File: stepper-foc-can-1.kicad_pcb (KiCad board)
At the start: 4 copper layers, 84 parts, among them J1 TC2030, J2 Conn_01x02, J3 Conn_01x04_Pin, J4 Conn_01x02, J5 Conn_01x02, M1 Stepper_Motor_bipolar, SW1 SW_Push, SW2 SW_Push, SW3 SW_Push, U1 STM32G474RBTx, U2 MX25947, U3 TPS62933, U4 TCAN3413, U5 AS5047P, U6 DRV8874, U7 INA241A3IDDF, U8 DRV8874, U9 INA241A3IDDF, Y1 Crystal_GND24

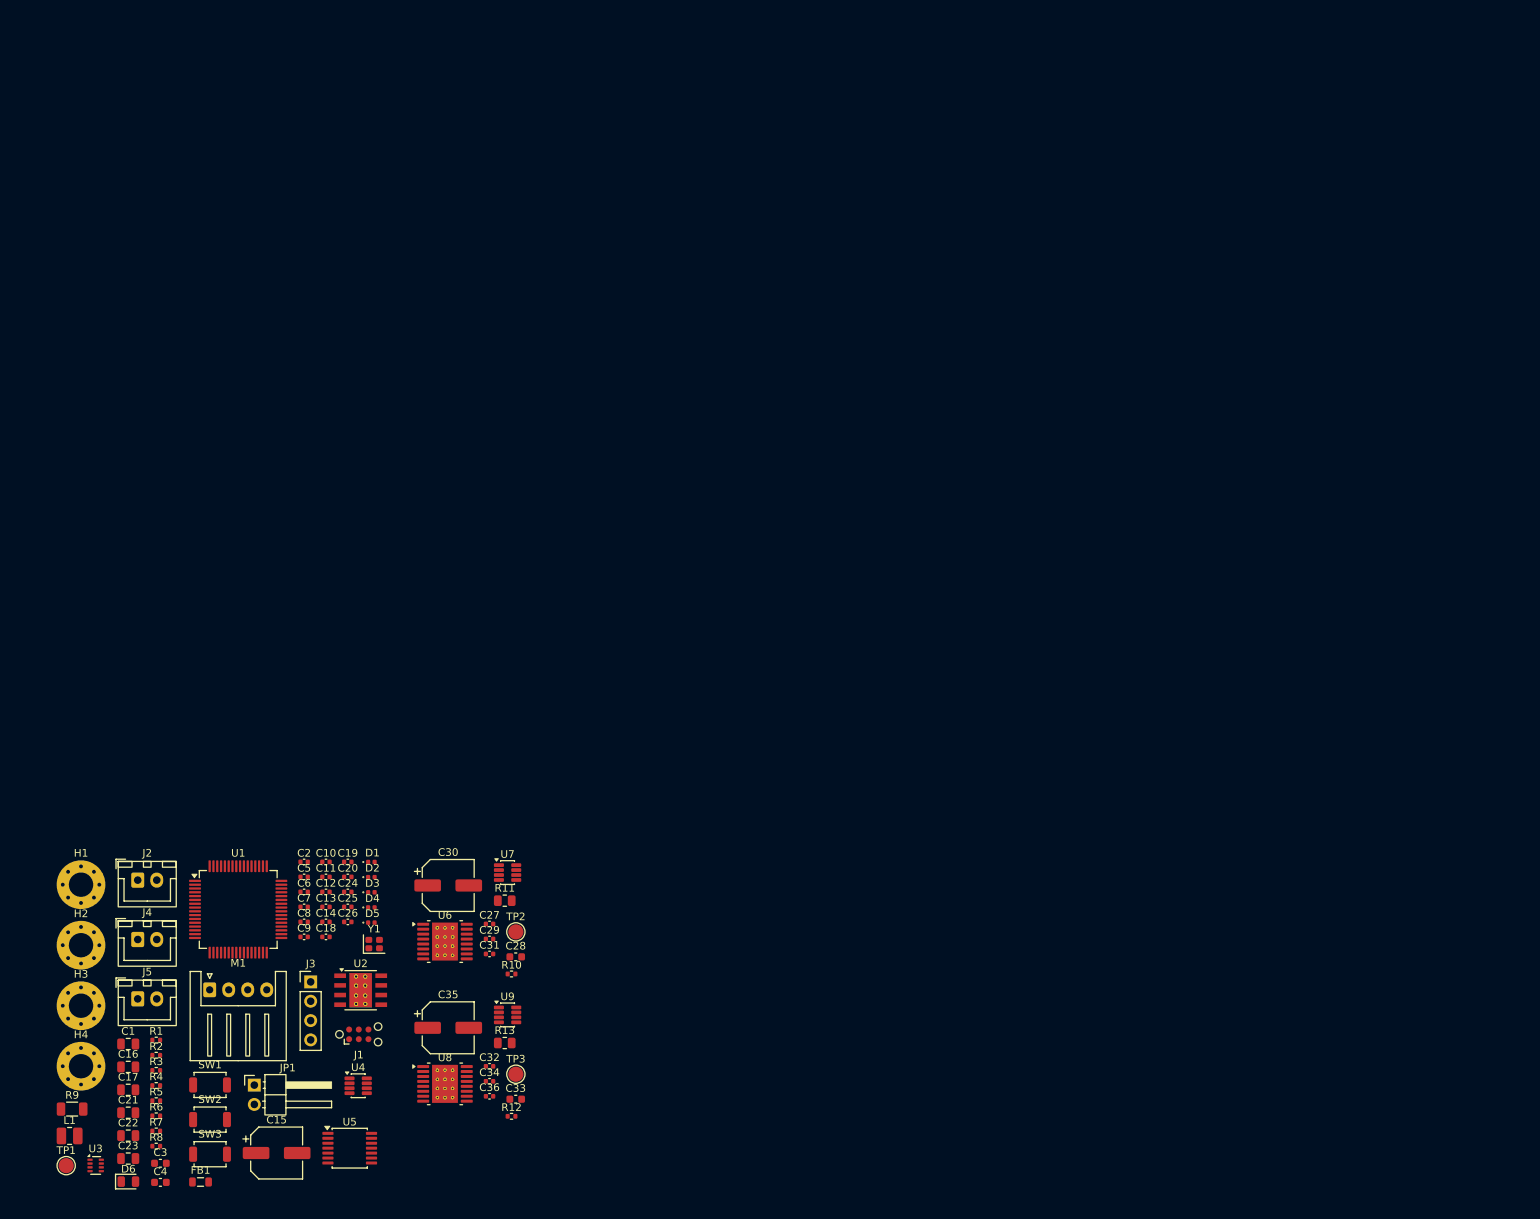
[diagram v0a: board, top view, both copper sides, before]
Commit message: pcb: add board outline
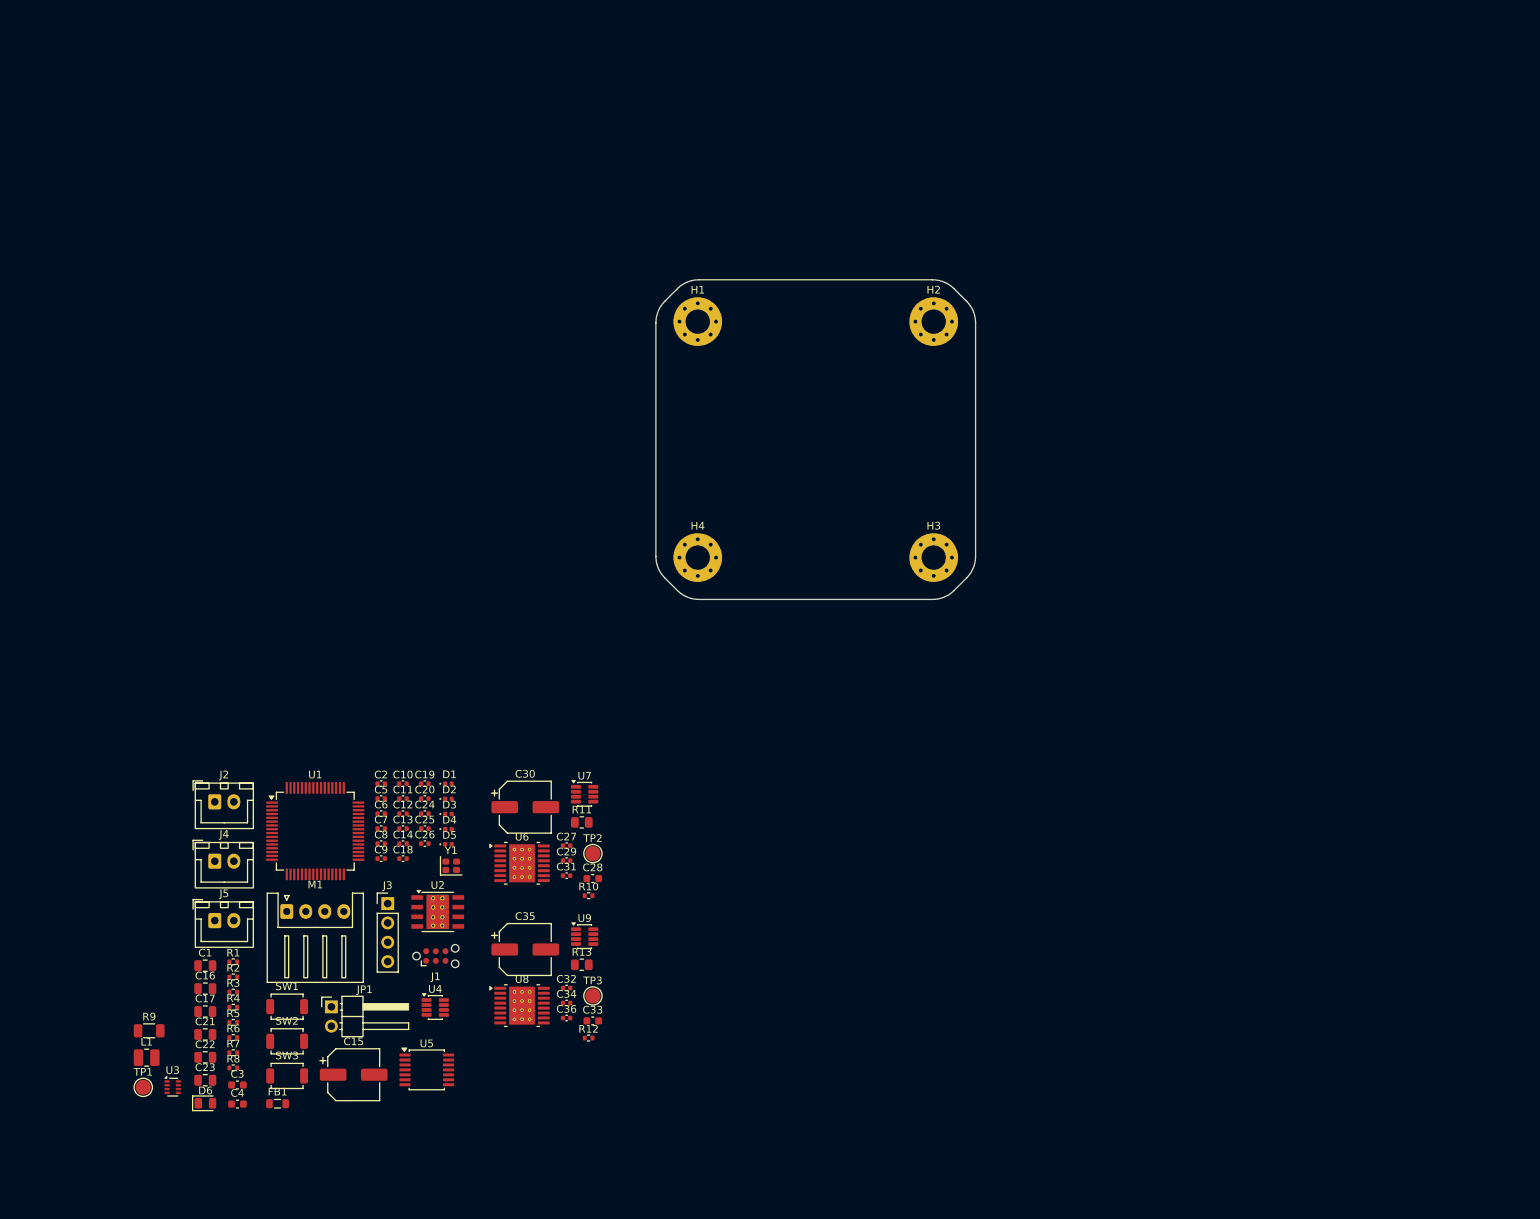
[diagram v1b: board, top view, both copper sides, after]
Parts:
- moved H2 138.8 mm to (159.5, 65.5)
- moved H3 126.6 mm to (159.5, 96.5)
- moved H1 109.7 mm to (128.5, 65.5)
- moved H4 105.0 mm to (128.5, 96.5)
- moved C11 14.4 mm to (89.8, 128.2)
- moved C12 14.4 mm to (89.8, 130.1)
- moved C17 14.4 mm to (63.8, 156.1)
- moved C20 14.4 mm to (92.7, 128.2)
- moved C23 14.4 mm to (63.8, 165.2)
- moved C24 14.4 mm to (92.7, 130.1)
- moved C28 14.4 mm to (114.7, 138.7)
- moved C5 14.4 mm to (86.9, 128.2)
- moved C6 14.4 mm to (86.9, 130.1)
- moved D2 14.4 mm to (95.7, 128.2)
- moved D5 14.4 mm to (95.7, 134.2)
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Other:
- board outline added: 42 x 42 mm

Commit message: pcb: add can layout
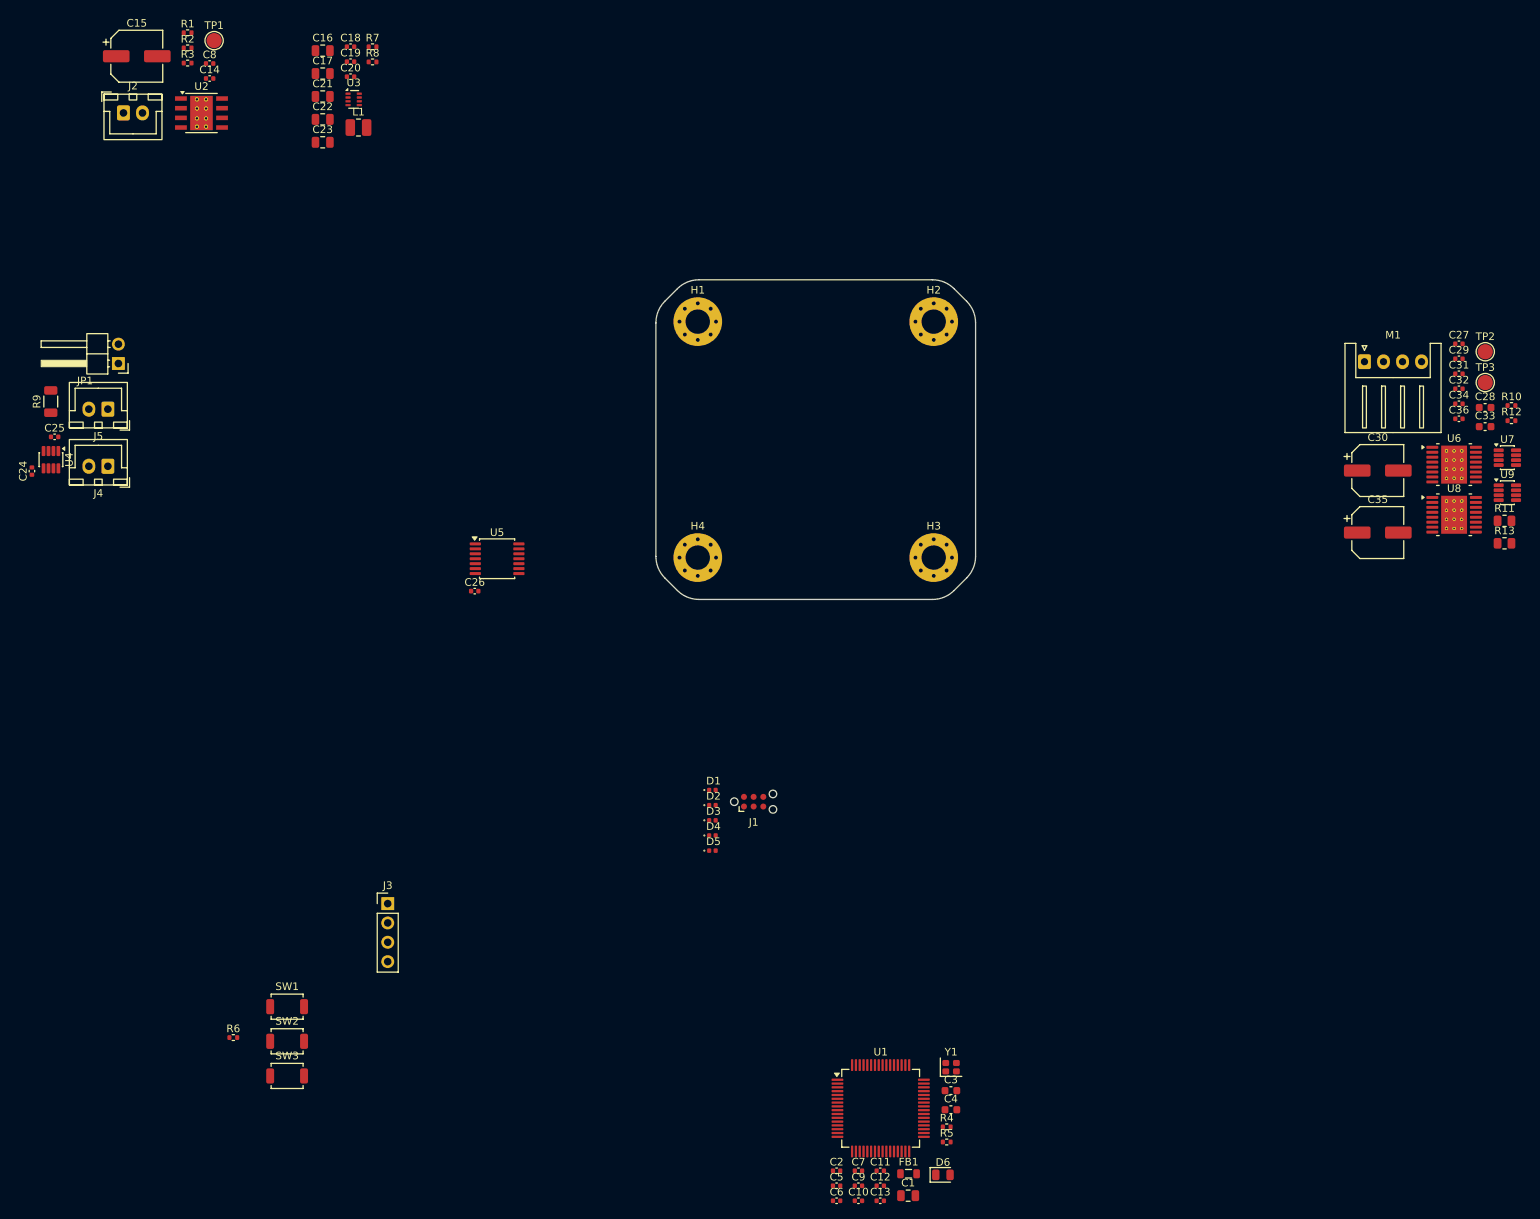
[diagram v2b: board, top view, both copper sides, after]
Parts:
- moved M1 159.0 mm to (216.1, 70.8)
- moved R12 145.9 mm to (235.4, 78.5)
- moved TP3 142.3 mm to (232.0, 73.5)
- moved C32 141.2 mm to (228.5, 74.3)
- moved C34 141.2 mm to (228.5, 76.3)
- moved C36 141.2 mm to (228.5, 78.3)
- moved C33 140.9 mm to (231.9, 79.3)
- moved U8 138.4 mm to (227.9, 90.9)
- moved TP1 137.8 mm to (65.0, 28.6)
- moved R10 137.3 mm to (235.4, 76.5)
- moved C15 136.8 mm to (54.8, 30.6)
- moved U9 134.5 mm to (234.9, 88.0)
- moved C27 134.5 mm to (228.5, 68.4)
- moved C29 134.5 mm to (228.5, 70.4)
- moved C31 134.5 mm to (228.5, 72.4)
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
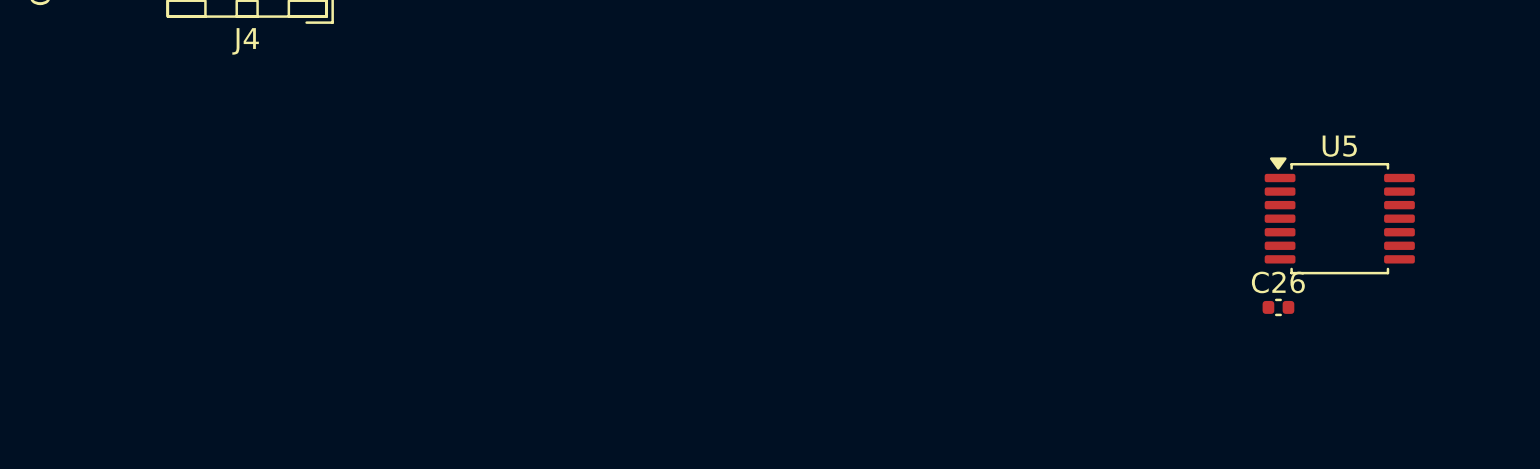
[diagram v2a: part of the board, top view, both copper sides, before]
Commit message: pcb: add hall sensor layout
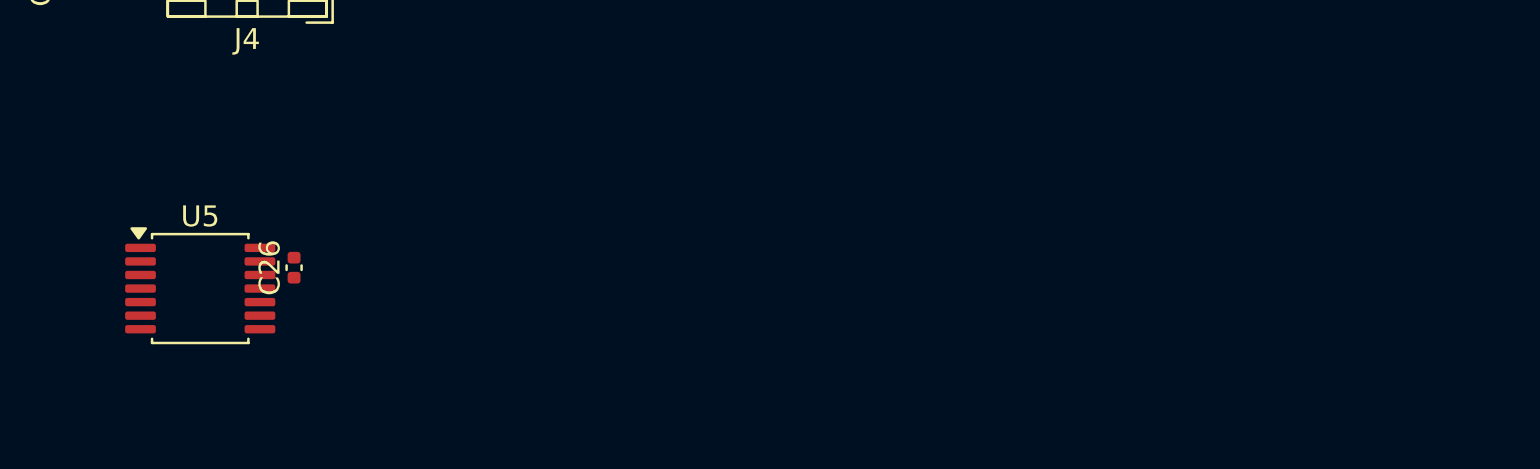
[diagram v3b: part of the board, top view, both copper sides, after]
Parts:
- moved U5 54.7 mm to (47.5, 100.0)
- moved C26 47.2 mm to (52.0, 99.0), turned to 90 degrees
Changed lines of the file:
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@@
 	(footprint "Package_SO:TSSOP-14_4.4x5mm_P0.65mm"
 		(layer "F.Cu")
-		(at 102.1375 96.65)
+		(at 47.5 100)
 		(descr "TSSOP, 14 Pin (JEDEC MO-153 variation AB-1, 1.00mm body thickness, https://www.jedec.org/document_search?search_api_views_fulltext=MO-153)")
 		(tags "TSSOP SO")
@@
 	(footprint "Capacitor_SMD:C_0402_1005Metric"
 		(layer "F.Cu")
-		(at 99.1975 100.905)
+		(at 52 99 90)
 		(descr "Capacitor SMD 0402 (1005 Metric), square (rectangular) end terminal, IPC-7351 nominal, (Body size source: IPC-SM-782 page 76, https://www.pcb-3d.com/wordpress/wp-content/uploads/ipc-sm-782a_amendment_1_and_2.pdf)")
 		(tags "capacitor")
 		(property "Reference" "C26"
-			(at 0 -1.16 0)
+			(at 0 -1.16 90)
 			(layer "F.SilkS")
 			(effects
@@
 		)
 		(property "Value" "0u1"
-			(at 0 1.16 0)
+			(at 0 1.16 90)
 			(layer "F.Fab")
 			(effects
@@
 		)
 		(property "Datasheet" ""
-			(at 0 0 0)
+			(at 0 0 90)
 			(layer "F.Fab")
 			(hide yes)
@@
 		)
 		(property "Description" "Unpolarized capacitor"
-			(at 0 0 0)
+			(at 0 0 90)
 			(layer "F.Fab")
 			(hide yes)
@@
 		)
 		(property "KiLib_Generator" "SMD_2terminal_chip_molded"
-			(at 0 0 0)
+			(at 0 0 90)
 			(layer "F.SilkS")
 			(hide yes)
@@
 		)
 		(property "Basic" "Y"
-			(at 0 0 0)
+			(at 0 0 90)
 			(unlocked yes)
 			(layer "F.Fab")
@@
 		)
 		(property "JLCPCB Part #" "C307331"
-			(at 0 0 0)
+			(at 0 0 90)
 			(unlocked yes)
 			(layer "F.Fab")
@@
 		)
 		(property "Manufacturer" "Samsung Electro-Mechanics "
-			(at 0 0 0)
+			(at 0 0 90)
 			(unlocked yes)
 			(layer "F.Fab")
@@
 		)
 		(property "Manufacturer Part Number" "CL05B104KB54PNC"
-			(at 0 0 0)
+			(at 0 0 90)
 			(unlocked yes)
 			(layer "F.Fab")
@@
 		)
 		(property "KLC_S3.3" ""
-			(at 0 0 0)
+			(at 0 0 90)
 			(unlocked yes)
 			(layer "F.Fab")
@@
 		)
 		(property "KLC_S4.1" ""
-			(at 0 0 0)
+			(at 0 0 90)
 			(unlocked yes)
 			(layer "F.Fab")
@@
 		)
 		(fp_text user "${REFERENCE}"
-			(at 0 0 0)
+			(at 0 0 90)
 			(layer "F.Fab")
 			(effects
@@
 		)
 		(pad "1" smd roundrect
-			(at -0.48 0)
+			(at -0.48 0 90)
 			(size 0.56 0.62)
 			(layers "F.Cu" "F.Mask" "F.Paste")
@@
 		)
 		(pad "2" smd roundrect
-			(at 0.48 0)
+			(at 0.48 0 90)
 			(size 0.56 0.62)
 			(layers "F.Cu" "F.Mask" "F.Paste")
